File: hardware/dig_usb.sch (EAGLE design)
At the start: 147 parts, among them IC1 AT90USB1287-AU, IC202 DS1337S, IC203 MAX487CSA, IC204 74HC166D, IC301 LTV-356T, IC302 LTV-356T, IC303 LTV-356T, IC304 LTV-356T, IC305 LTV-356T, IC306 LTV-356T, IC307 LTV-356T, IC308 LTV-356T, K401 S202S02, K402 S202S02, K403 S202S02, K404 S202S02, K405 S202S02, K406 S202S02, K407 S202S02, K408 S202S02, Q201 32,768kHz, T301 BCR191, T302 BCR191, T303 BCR191, T304 BCR191, T305 BCR191, T306 BCR191, T307 BCR191, T308 BCR191, X101 RIA-73-02, X201 ISP, X202 RIA-73-02, X301 RIA-73-02, X302 RIA-73-02, X303 RIA-73-02, X304 RIA-73-02, X305 RIA-73-02, X401 RIA-73-02, X402 RIA-73-02, X403 RIA-73-02, X404 RIA-73-02, X405 RIA-73-02

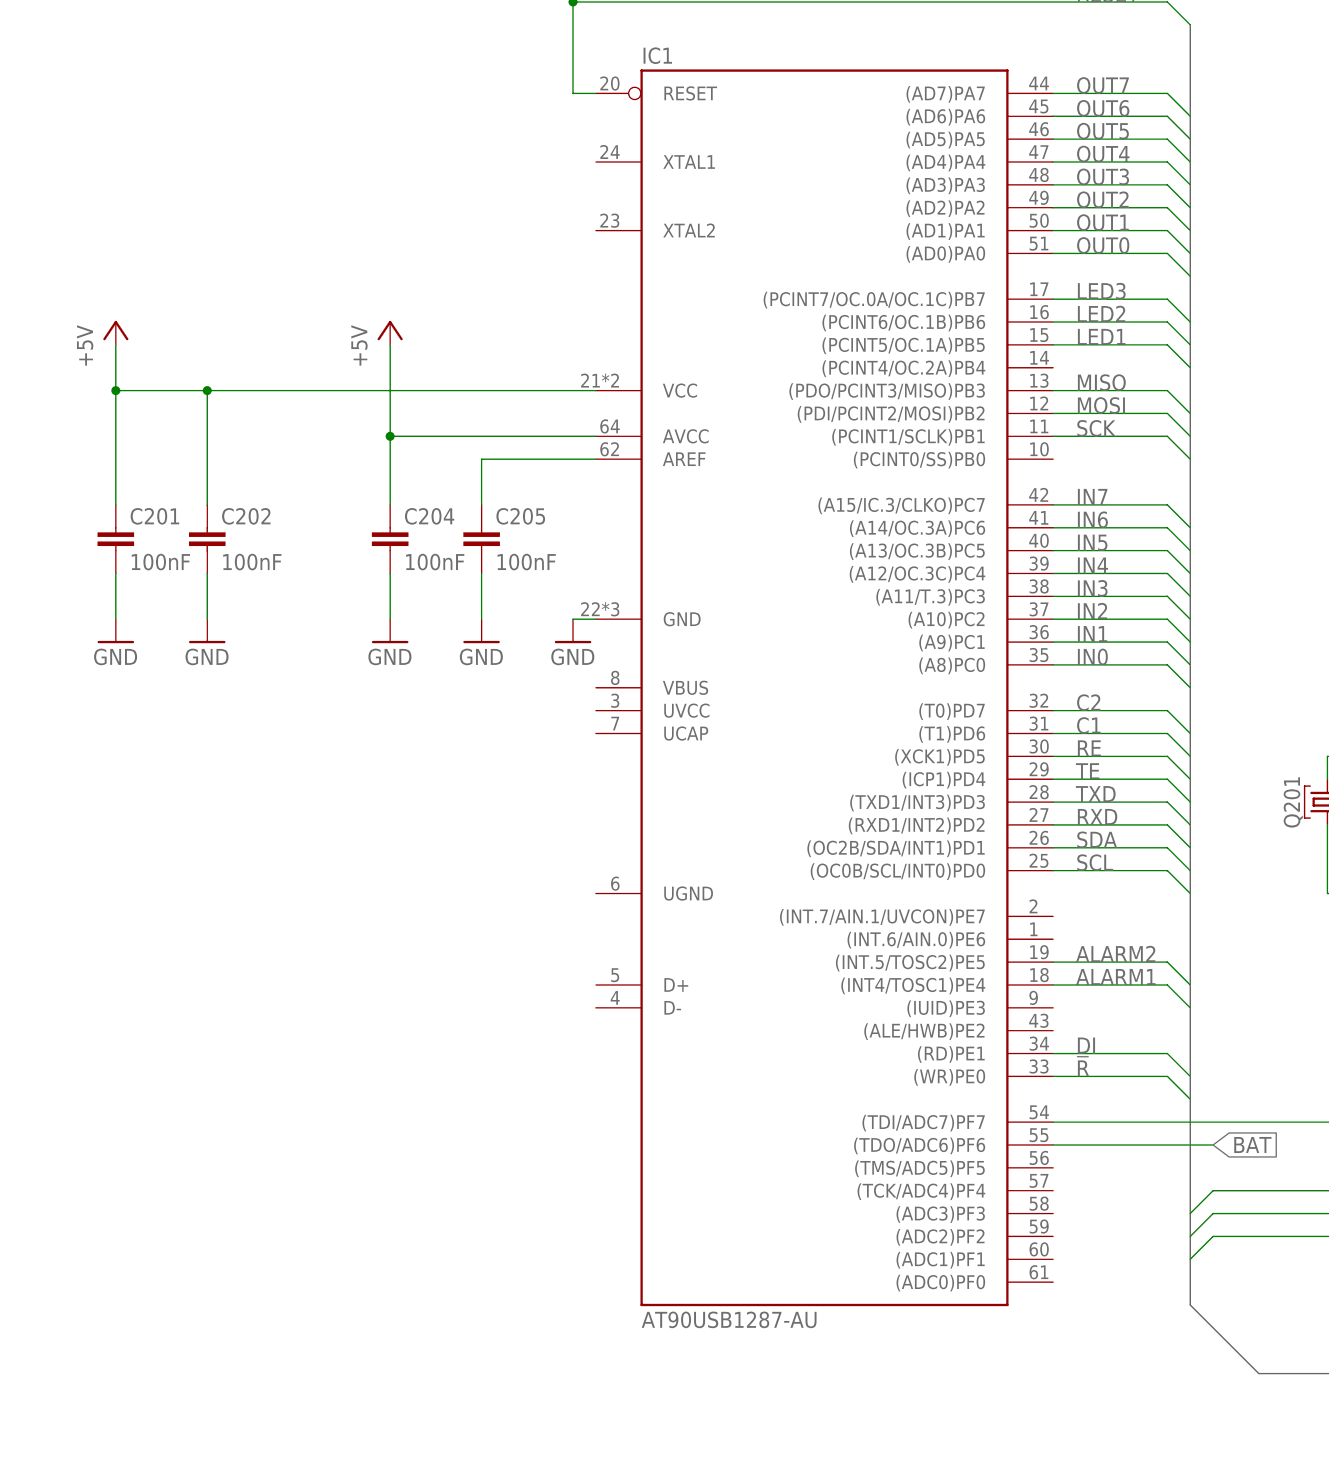
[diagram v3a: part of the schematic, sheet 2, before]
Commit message: USB Stecker und Quarz hinzugefügt
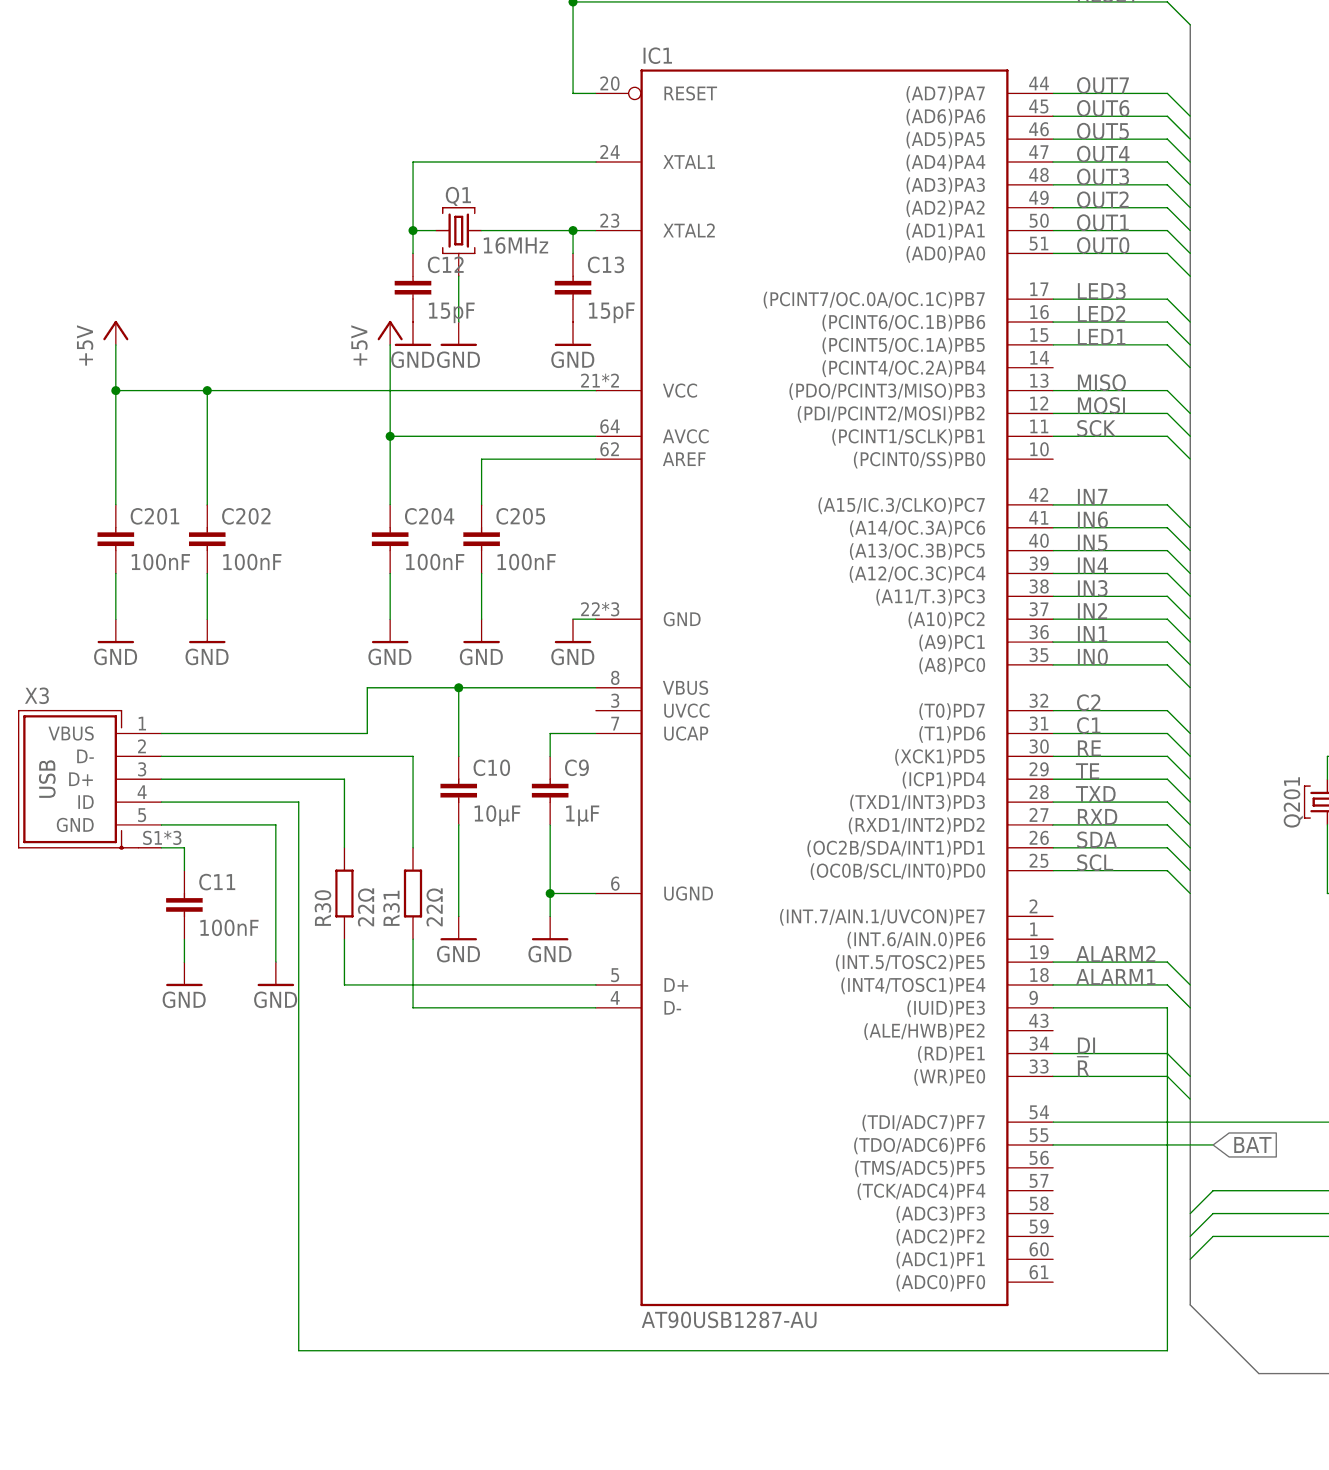
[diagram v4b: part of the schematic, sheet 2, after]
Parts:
- added C10: 10μF, passiv:C_0805
- added C11: 100nF, passiv:C_0805
- added C12, C13: 15pF, passiv:C_0805
- added C9: 1μF, passiv:C_0805
- added Q1: 16MHz, passiv:QM_X22
- added R30, R31: 22Ω, passiv:R_0805
- added X3: (no value), stecker:USB-MICRO-SMD-V
- Q201: device passiv:QM_ -> passiv:QM_MS1V-T1K
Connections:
- new net N$118: C9.1, IC1.UCAP
- new net N$119: R30.2, X3.D+
- new net N$120: IC1.D+, R30.1
- new net N$121: R31.2, X3.D-
- new net N$122: IC1.D-, R31.1
- new net N$123: IC1.(IUID)PE3, X3.ID
- new net N$124: C10.1, IC1.VBUS, X3.VBUS
- new net N$125: C13.1, IC1.XTAL2, Q1.2
- new net N$128: C12.1, IC1.XTAL1, Q1.1
- new net USHIELD: C11.1, X3.SHIELD
- net GND: now also C10.2, C11.2, C12.2, C13.2, C9.2, IC1.UGND, Q1.G, X3.GND
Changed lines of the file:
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@@
 <part name="GND42" library="versorgung" deviceset="GND" device=""/>
 <part name="IC202" library="ic-controller" deviceset="DS1337" device="S"/>
-<part name="Q201" library="passiv" deviceset="QM_" device="" value="32,768kHz"/>
+<part name="Q201" library="passiv" deviceset="QM_" device="MS1V-T1K" value="32,768kHz"/>
 <part name="C104" library="passiv" deviceset="C_" device="0603" value="100nF"/>
 <part name="GND45" library="versorgung" deviceset="GND" device=""/>
@@
 <part name="R29" library="widerstandsnetzwerk" deviceset="EXB-38V" device="" value="1,5kΩ"/>
 <part name="P+9" library="versorgung" deviceset="+5V" device=""/>
+<part name="C9" library="passiv" deviceset="C_" device="0805" value="1μF"/>
+<part name="GND67" library="versorgung" deviceset="GND" device=""/>
+<part name="X3" library="stecker" deviceset="USB-MICRO" device="-SMD-V"/>
+<part name="R30" library="passiv" deviceset="R_" device="0805" value="22Ω"/>
+<part name="R31" library="passiv" deviceset="R_" device="0805" value="22Ω"/>
+<part name="GND68" library="versorgung" deviceset="GND" device=""/>
+<part name="C10" library="passiv" deviceset="C_" device="0805" value="10μF"/>
+<part name="GND69" library="versorgung" deviceset="GND" device=""/>
+<part name="C11" library="passiv" deviceset="C_" device="0805" value="100nF"/>
+<part name="GND70" library="versorgung" deviceset="GND" device=""/>
+<part name="Q1" library="passiv" deviceset="QM_" device="X22" value="16MHz"/>
+<part name="C12" library="passiv" deviceset="C_" device="0805" value="15pF"/>
+<part name="C13" library="passiv" deviceset="C_" device="0805" value="15pF"/>
+<part name="GND71" library="versorgung" deviceset="GND" device=""/>
+<part name="GND72" library="versorgung" deviceset="GND" device=""/>
+<part name="GND73" library="versorgung" deviceset="GND" device=""/>
 </parts>
 <sheets>
@@
 <instance part="GND41" gate="1" x="256.54" y="10.16"/>
 <instance part="P+9" gate="1" x="241.3" y="55.88"/>
+<instance part="C9" gate="G$1" x="68.58" y="81.28"/>
+<instance part="GND67" gate="1" x="68.58" y="63.5"/>
+<instance part="X3" gate="G$1" x="15.24" y="81.28"/>
+<instance part="R30" gate="G$1" x="45.72" y="68.58" rot="R90"/>
+<instance part="R31" gate="G$1" x="53.34" y="68.58" rot="R90"/>
+<instance part="GND68" gate="1" x="38.1" y="58.42"/>
+<instance part="C10" gate="G$1" x="58.42" y="81.28"/>
+<instance part="GND69" gate="1" x="58.42" y="63.5"/>
+<instance part="C11" gate="G$1" x="27.94" y="68.58"/>
+<instance part="GND70" gate="1" x="27.94" y="58.42"/>
+<instance part="Q1" gate="G$1" x="58.42" y="142.24"/>
+<instance part="C12" gate="G$1" x="53.34" y="137.16"/>
+<instance part="C13" gate="G$1" x="71.12" y="137.16"/>
+<instance part="GND71" gate="1" x="53.34" y="129.54"/>
+<instance part="GND72" gate="1" x="58.42" y="129.54"/>
+<instance part="GND73" gate="1" x="71.12" y="129.54"/>
 </instances>
 <busses>
@@
 <pinref part="GND41" gate="1" pin="GND"/>
 </segment>
+<segment>
+<pinref part="C9" gate="G$1" pin="2"/>
+<pinref part="GND67" gate="1" pin="GND"/>
+<wire x1="68.58" y1="66.04" x2="68.58" y2="68.58" width="0.1524" layer="91"/>
+<pinref part="IC1" gate="G$1" pin="UGND"/>
+<wire x1="68.58" y1="68.58" x2="68.58" y2="76.2" width="0.1524" layer="91"/>
+<wire x1="73.66" y1="68.58" x2="68.58" y2="68.58" width="0.1524" layer="91"/>
+<junction x="68.58" y="68.58"/>
+</segment>
+<segment>
+<pinref part="X3" gate="G$1" pin="GND"/>
+<pinref part="GND68" gate="1" pin="GND"/>
+<wire x1="25.4" y1="76.2" x2="38.1" y2="76.2" width="0.1524" layer="91"/>
+<wire x1="38.1" y1="76.2" x2="38.1" y2="60.96" width="0.1524" layer="91"/>
+</segment>
+<segment>
+<pinref part="GND69" gate="1" pin="GND"/>
+<pinref part="C10" gate="G$1" pin="2"/>
+<wire x1="58.42" y1="66.04" x2="58.42" y2="76.2" width="0.1524" layer="91"/>
+</segment>
+<segment>
+<pinref part="GND70" gate="1" pin="GND"/>
+<pinref part="C11" gate="G$1" pin="2"/>
+<wire x1="27.94" y1="60.96" x2="27.94" y2="63.5" width="0.1524" layer="91"/>
+</segment>
+<segment>
+<pinref part="C12" gate="G$1" pin="2"/>
+<pinref part="GND71" gate="1" pin="GND"/>
+</segment>
+<segment>
+<pinref part="C13" gate="G$1" pin="2"/>
+<pinref part="GND73" gate="1" pin="GND"/>
+</segment>
+<segment>
+<pinref part="Q1" gate="G$1" pin="G"/>
+<pinref part="GND72" gate="1" pin="GND"/>
+<wire x1="58.42" y1="137.16" x2="58.42" y2="132.08" width="0.1524" layer="91"/>
+</segment>
 </net>
 <net name="+5V" class="0">
@@
 </segment>
 </net>
+<net name="N$118" class="0">
+<segment>
+<pinref part="IC1" gate="G$1" pin="UCAP"/>
+<pinref part="C9" gate="G$1" pin="1"/>
+<wire x1="73.66" y1="86.36" x2="68.58" y2="86.36" width="0.1524" layer="91"/>
+<wire x1="68.58" y1="86.36" x2="68.58" y2="83.82" width="0.1524" layer="91"/>
+</segment>
+</net>
+<net name="N$119" class="0">
+<segment>
+<pinref part="X3" gate="G$1" pin="D+"/>
+<pinref part="R30" gate="G$1" pin="2"/>
+<wire x1="25.4" y1="81.28" x2="45.72" y2="81.28" width="0.1524" layer="91"/>
+<wire x1="45.72" y1="81.28" x2="45.72" y2="73.66" width="0.1524" layer="91"/>
+</segment>
+</net>
+<net name="N$120" class="0">
+<segment>
+<pinref part="R30" gate="G$1" pin="1"/>
+<pinref part="IC1" gate="G$1" pin="D+"/>
+<wire x1="45.72" y1="63.5" x2="45.72" y2="58.42" width="0.1524" layer="91"/>
+<wire x1="45.72" y1="58.42" x2="73.66" y2="58.42" width="0.1524" layer="91"/>
+</segment>
+</net>
+<net name="N$121" class="0">
+<segment>
+<pinref part="X3" gate="G$1" pin="D-"/>
+<pinref part="R31" gate="G$1" pin="2"/>
+<wire x1="25.4" y1="83.82" x2="53.34" y2="83.82" width="0.1524" layer="91"/>
+<wire x1="53.34" y1="83.82" x2="53.34" y2="73.66" width="0.1524" layer="91"/>
+</segment>
+</net>
+<net name="N$122" class="0">
+<segment>
+<pinref part="R31" gate="G$1" pin="1"/>
+<pinref part="IC1" gate="G$1" pin="D-"/>
+<wire x1="53.34" y1="63.5" x2="53.34" y2="55.88" width="0.1524" layer="91"/>
+<wire x1="53.34" y1="55.88" x2="73.66" y2="55.88" width="0.1524" layer="91"/>
+</segment>
+</net>
+<net name="N$123" class="0">
+<segment>
+<pinref part="IC1" gate="G$1" pin="(IUID)PE3"/>
+<wire x1="124.46" y1="55.88" x2="137.16" y2="55.88" width="0.1524" layer="91"/>
+<wire x1="137.16" y1="55.88" x2="137.16" y2="17.78" width="0.1524" layer="91"/>
+<wire x1="137.16" y1="17.78" x2="40.64" y2="17.78" width="0.1524" layer="91"/>
+<wire x1="40.64" y1="17.78" x2="40.64" y2="78.74" width="0.1524" layer="91"/>
+<pinref part="X3" gate="G$1" pin="ID"/>
+<wire x1="40.64" y1="78.74" x2="25.4" y2="78.74" width="0.1524" layer="91"/>
+</segment>
+</net>
+<net name="N$124" class="0">
+<segment>
+<pinref part="IC1" gate="G$1" pin="VBUS"/>
+<wire x1="73.66" y1="91.44" x2="58.42" y2="91.44" width="0.1524" layer="91"/>
+<wire x1="58.42" y1="91.44" x2="48.26" y2="91.44" width="0.1524" layer="91"/>
+<wire x1="48.26" y1="91.44" x2="48.26" y2="86.36" width="0.1524" layer="91"/>
+<pinref part="X3" gate="G$1" pin="VBUS"/>
+<wire x1="48.26" y1="86.36" x2="25.4" y2="86.36" width="0.1524" layer="91"/>
+<pinref part="C10" gate="G$1" pin="1"/>
+<wire x1="58.42" y1="83.82" x2="58.42" y2="91.44" width="0.1524" layer="91"/>
+<junction x="58.42" y="91.44"/>
+</segment>
+</net>
+<net name="USHIELD" class="0">
+<segment>
+<pinref part="C11" gate="G$1" pin="1"/>
+<pinref part="X3" gate="G$1" pin="SHIELD"/>
+<wire x1="27.94" y1="71.12" x2="27.94" y2="73.66" width="0.1524" layer="91"/>
+<wire x1="27.94" y1="73.66" x2="25.4" y2="73.66" width="0.1524" layer="91"/>
+</segment>
+</net>
+<net name="N$125" class="0">
+<segment>
+<pinref part="IC1" gate="G$1" pin="XTAL2"/>
+<pinref part="Q1" gate="G$1" pin="2"/>
+<wire x1="73.66" y1="142.24" x2="71.12" y2="142.24" width="0.1524" layer="91"/>
+<pinref part="C13" gate="G$1" pin="1"/>
+<wire x1="71.12" y1="142.24" x2="60.96" y2="142.24" width="0.1524" layer="91"/>
+<wire x1="71.12" y1="139.7" x2="71.12" y2="142.24" width="0.1524" layer="91"/>
+<junction x="71.12" y="142.24"/>
+</segment>
+</net>
+<net name="N$128" class="0">
+<segment>
+<pinref part="Q1" gate="G$1" pin="1"/>
+<wire x1="55.88" y1="142.24" x2="53.34" y2="142.24" width="0.1524" layer="91"/>
+<wire x1="53.34" y1="142.24" x2="53.34" y2="149.86" width="0.1524" layer="91"/>
+<pinref part="IC1" gate="G$1" pin="XTAL1"/>
+<wire x1="53.34" y1="149.86" x2="73.66" y2="149.86" width="0.1524" layer="91"/>
+<pinref part="C12" gate="G$1" pin="1"/>
+<wire x1="53.34" y1="142.24" x2="53.34" y2="139.7" width="0.1524" layer="91"/>
+<junction x="53.34" y="142.24"/>
+</segment>
+</net>
